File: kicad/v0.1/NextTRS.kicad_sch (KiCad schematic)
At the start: 95 parts, among them J1 TRS-80 M3 Pin Header, J10 AudioJack3, J11 Mini-DIN-6, J12 USB_B_Micro, J2 TRS-80 M1 Pin Connector, J3 TRS-80 M3 Edge Connector, J4 TRS-80 M1 Edge Connector, J5 Conn_01x06_Male, J6 Conn_01x06_Male, J7 HDMI_A, J8 Programmer, J9 SD_Card, Q1 MMBT3904, Q2 MMBT3904, Q3 2N7002, Q4 2N7002, Q5 2N7002, SW1 ESP_RESET, SW2 PTRS_RESET/STATUS, SW3 SW_DIP_x04, U1 ESP32-WROVER-B, U2 74LVC245, U3 74LVC245, U4 74LVC245, U5 74LVC245, U6 74LVC245

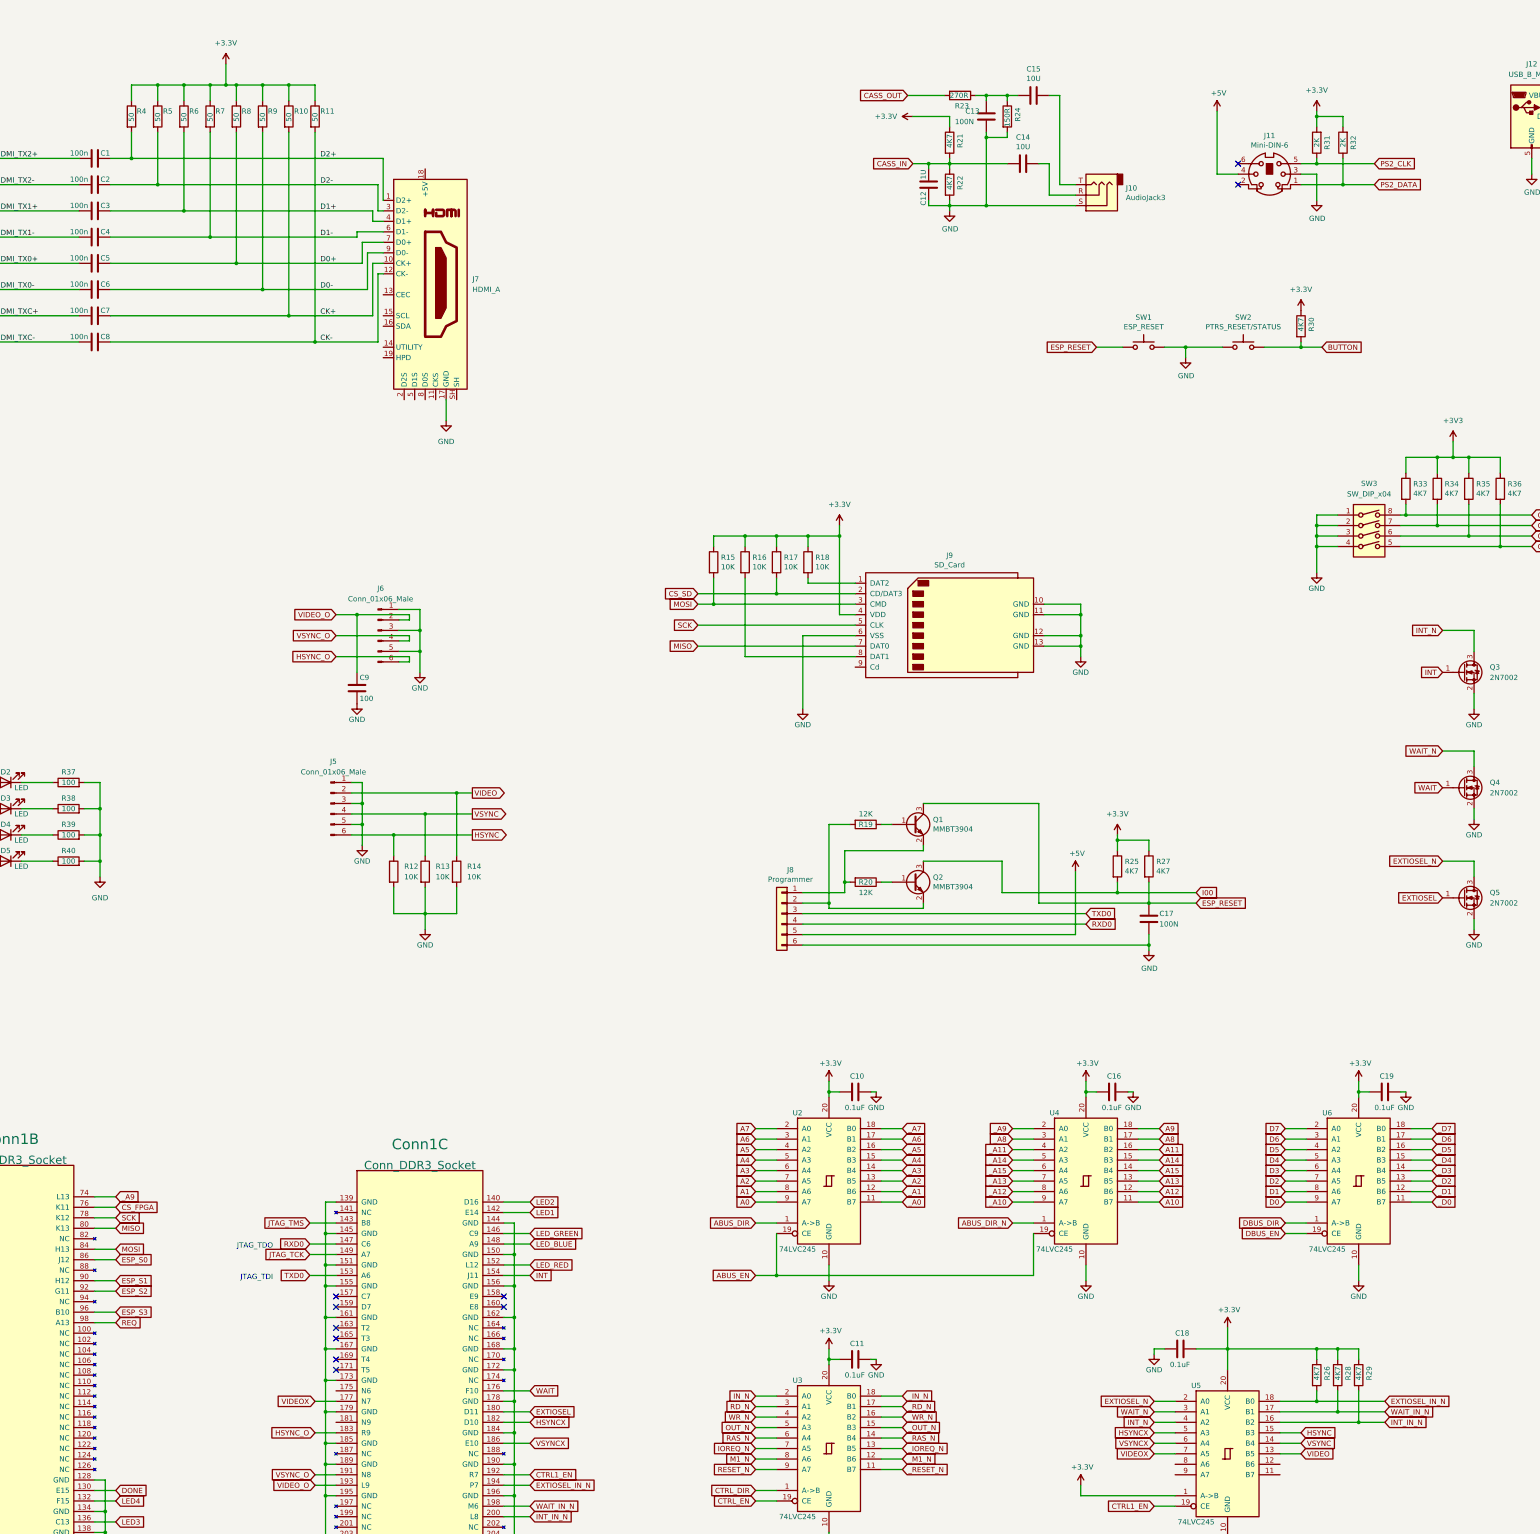
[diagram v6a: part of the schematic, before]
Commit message: Added HDMI shield grounds. Added ground pour under Nano socket. Correced U5 connections.
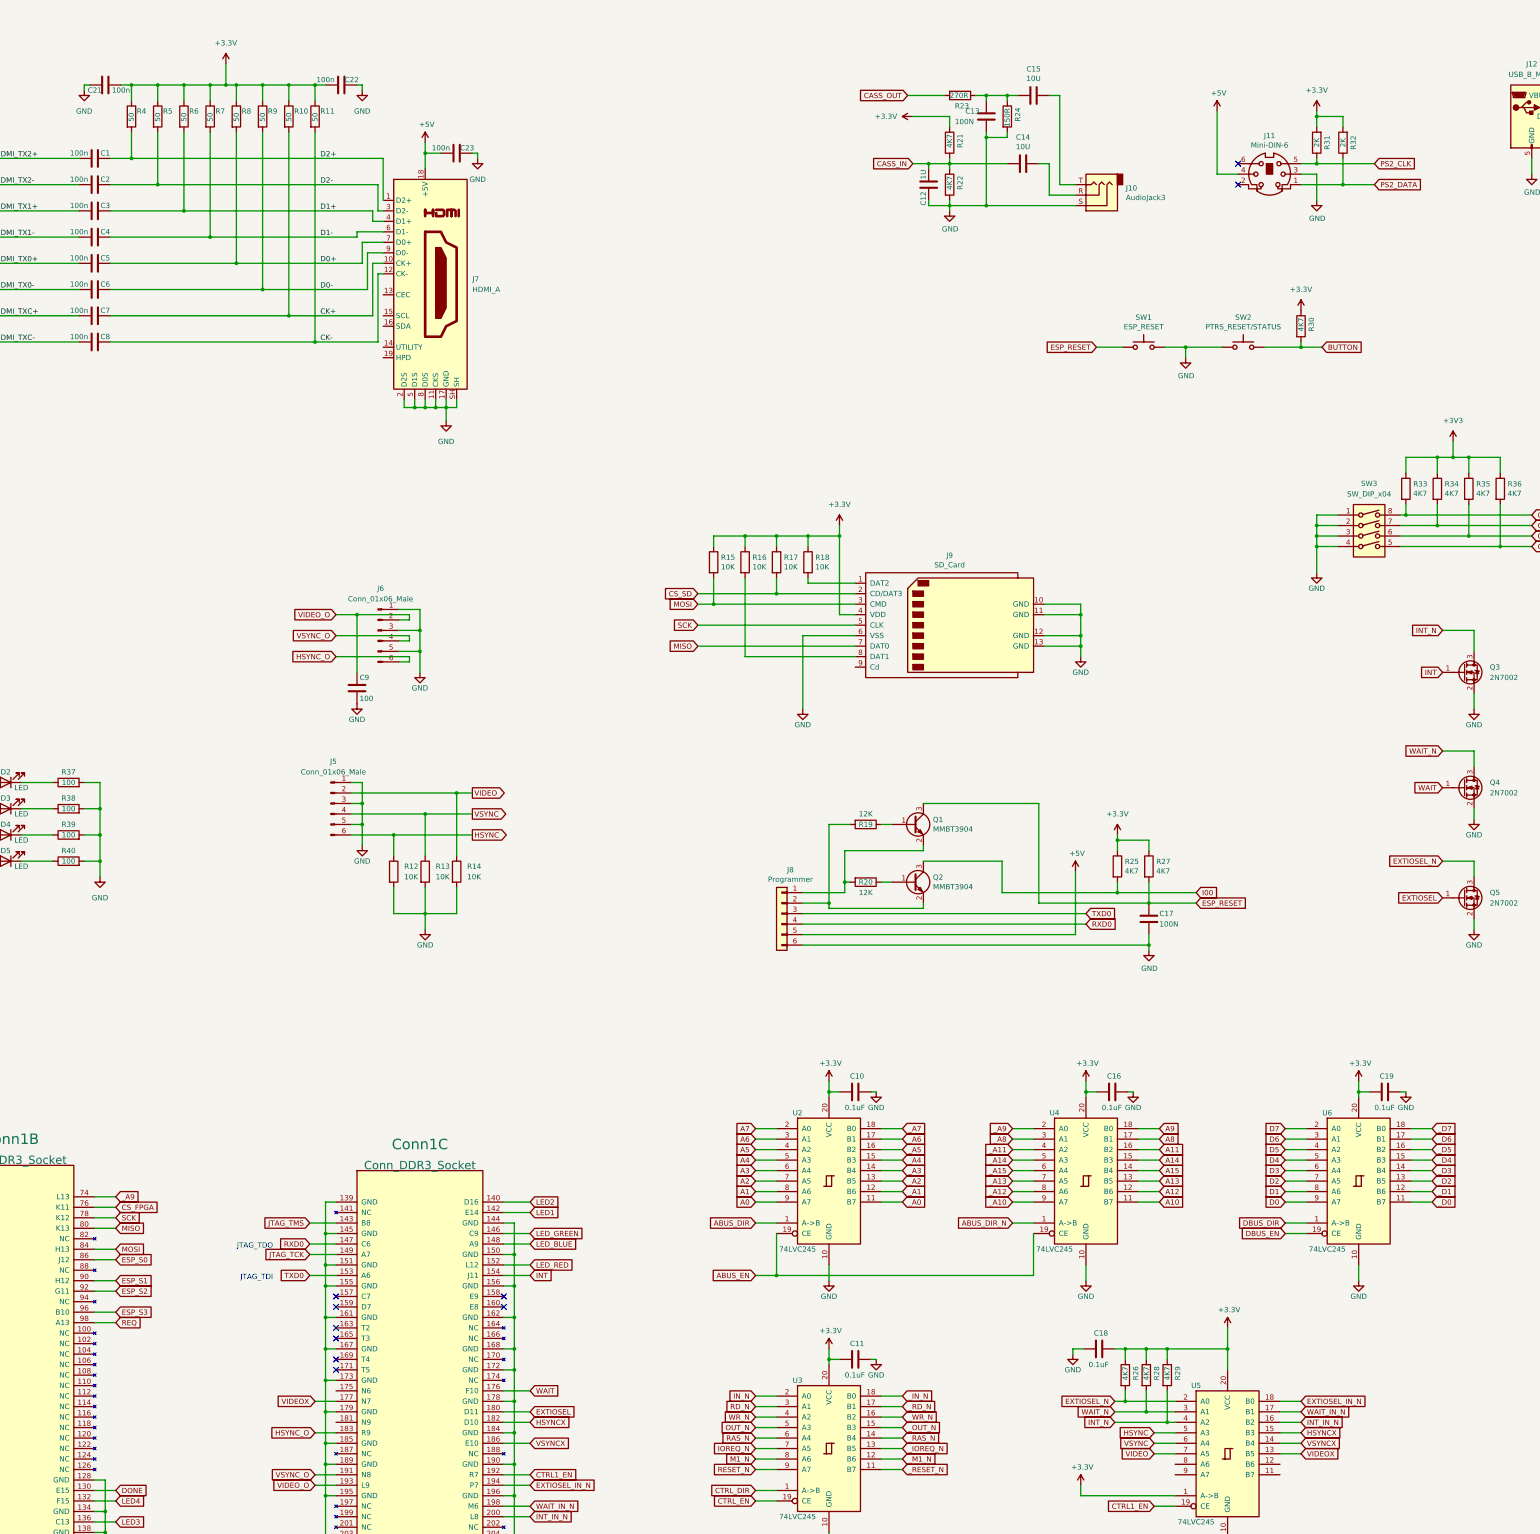
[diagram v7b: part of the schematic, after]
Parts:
- added C21, C22, C23: 100n, Capacitor_SMD:C_0805_2012Metric_Pad1.18x1.45mm_HandSolder, symbol Device:C
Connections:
- net +3.3V: now also C21.1, C22.1
- net +5V: now also J7.18 (+5V), C23.1
- net EXTIOSEL_IN_N: no longer R26.2
- net EXTIOSEL_N: now also R26.2
- net GND: now also J7.11 (CKS), J7.2 (D2S), J7.5 (D1S), J7.8 (D0S), J7.SH, C21.2, C22.2, C23.2
- net HSYNC: now also U5.5 (A3); no longer U5.15 (B3)
- net HSYNCX: now also U5.15 (B3); no longer U5.5 (A3)
- net INT_IN_N: no longer R29.2
- net INT_N: now also R29.2
- net VIDEO: now also U5.7 (A5); no longer U5.13 (B5)
- net VIDEOX: now also U5.13 (B5); no longer U5.7 (A5)
- net VSYNC: now also U5.6 (A4); no longer U5.14 (B4)
- net VSYNCX: now also U5.14 (B4); no longer U5.6 (A4)
- net WAIT_IN_N: no longer R28.2
- net WAIT_N: now also R28.2
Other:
- moved on the sheet: C18, R26, R28, R29

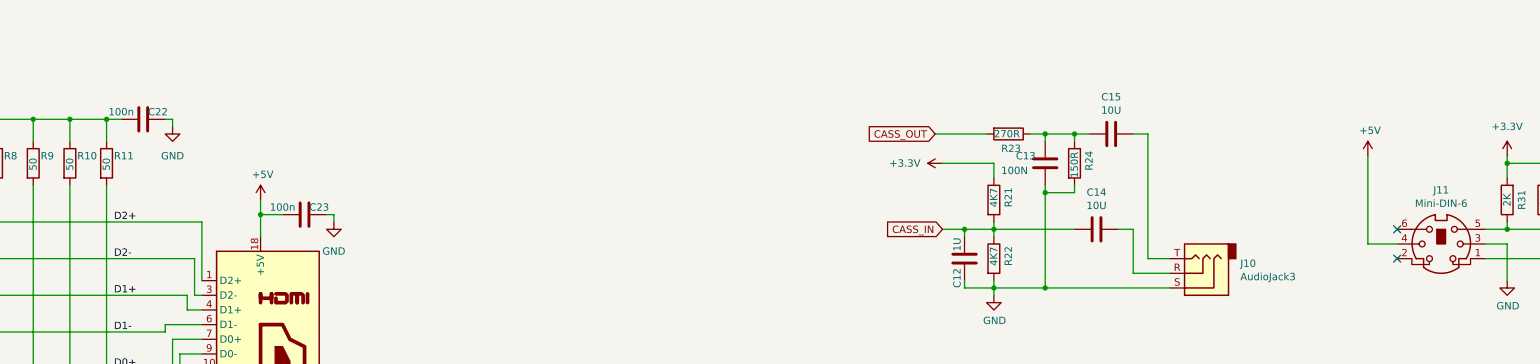
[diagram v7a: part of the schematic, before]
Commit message: Moved HDMI termination Rs. Added HDMI shield grounds.
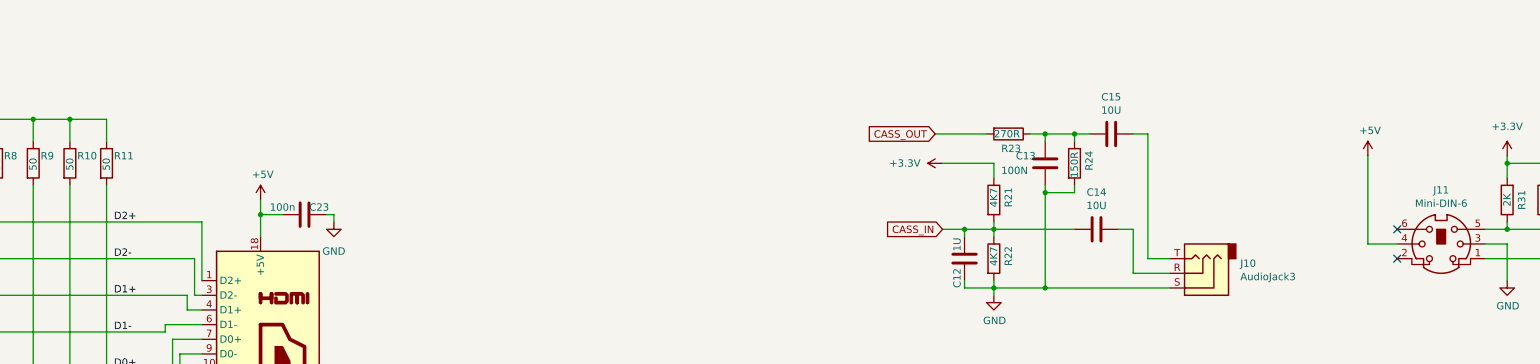
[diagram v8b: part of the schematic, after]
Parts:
- removed C22: 100n, Capacitor_SMD:C_0805_2012Metric_Pad1.18x1.45mm_HandSolder, symbol Device:C
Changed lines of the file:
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@@
   (junction (at 447.04 99.06) (diameter 0) (color 0 0 0 0)
   )
-  (junction (at 236.22 35.56) (diameter 0) (color 0 0 0 0)
-  )
   (junction (at 184.15 223.52) (diameter 0) (color 0 0 0 0)
   )
@@
     (stroke (width 0) (type default) (color 0 0 0 0))
   )
-  (wire (pts (xy 247.65 35.56) (xy 247.65 36.83))
-    (stroke (width 0) (type default) (color 0 0 0 0))
-  )
   (wire (pts (xy 137.16 342.9) (xy 142.24 342.9))
     (stroke (width 0) (type default) (color 0 0 0 0))
@@
     (stroke (width 0) (type default) (color 0 0 0 0))
   )
-  (wire (pts (xy 246.38 35.56) (xy 247.65 35.56))
-    (stroke (width 0) (type default) (color 0 0 0 0))
-  )
   (wire (pts (xy 412.75 161.29) (xy 421.64 161.29))
     (stroke (width 0) (type default) (color 0 0 0 0))
@@
     (stroke (width 0) (type default) (color 0 0 0 0))
   )
-  (wire (pts (xy 236.22 35.56) (xy 238.76 35.56))
-    (stroke (width 0) (type default) (color 0 0 0 0))
-  )
   (wire (pts (xy 422.91 238.76) (xy 354.33 238.76))
     (stroke (width 0) (type default) (color 0 0 0 0))
@@
     (pin "1")
   )
-  (symbol (lib_id "power:GND") (at 247.65 36.83 0) (unit 1)
-    (in_bom yes) (on_board yes) (fields_autoplaced)
-    (property "Reference" "#PWR0107" (id 0) (at 247.65 43.18 0)
-      (effects (font (size 1.27 1.27)) hide)
-    )
-    (property "Value" "GND" (id 1) (at 247.65 41.91 0))
-    (property "Footprint" "" (id 2) (at 247.65 36.83 0)
-      (effects (font (size 1.27 1.27)) hide)
-    )
-    (property "Datasheet" "" (id 3) (at 247.65 36.83 0)
-      (effects (font (size 1.27 1.27)) hide)
-    )
-    (pin "1")
-  )
   (symbol (lib_id "power:GND") (at 516.89 213.36 0) (unit 1)
     (in_bom yes) (on_board yes)
@@
     (pin "1")
   )
-  (symbol (lib_id "Device:C") (at 242.57 35.56 90) (unit 1)
-    (in_bom yes) (on_board yes)
-    (property "Reference" "C22" (id 0) (at 245.11 34.29 90))
-    (property "Value" "100n" (id 1) (at 238.76 34.29 90))
-    (property "Footprint" "Capacitor_SMD:C_0805_2012Metric_Pad1.18x1.45mm_HandSolder" (id 2) (at 246.38 34.5948 0)
-      (effects (font (size 1.27 1.27)) hide)
-    )
-    (property "Datasheet" "~" (id 3) (at 242.57 35.56 0)
-      (effects (font (size 1.27 1.27)) hide)
-    )
-    (pin "1")
-    (pin "2")
-  )
   (symbol (lib_id "SDCard:SD_Card") (at 389.89 166.37 0) (unit 1)
     (in_bom yes) (on_board yes)
@@
       (reference "#PWR0106") (unit 1) (value "+3V3") (footprint "")
     )
-    (path "/20ff2a52-1fdf-4f96-af9a-dfeb22c389ac"
-      (reference "#PWR0107") (unit 1) (value "GND") (footprint "")
-    )
     (path "/d1e2bfa4-f851-4d3d-87e5-bd6b043483b2"
       (reference "#PWR0108") (unit 1) (value "GND") (footprint "")
@@
       (reference "C21") (unit 1) (value "100n") (footprint "Capacitor_SMD:C_0805_2012Metric_Pad1.18x1.45mm_HandSolder")
     )
-    (path "/2d7a87a4-5481-4355-9eac-e1b2169cdce3"
-      (reference "C22") (unit 1) (value "100n") (footprint "Capacitor_SMD:C_0805_2012Metric_Pad1.18x1.45mm_HandSolder")
-    )
     (path "/d430ea7e-1ca5-408e-840e-7c298c3acded"
